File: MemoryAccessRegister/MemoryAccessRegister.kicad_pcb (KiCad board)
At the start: 2 copper layers, 75.8 x 38.8 mm, 20 parts, among them J1 Conn_01x04_Pin, J2 Conn_01x04_Pin, J3 Conn_01x06_Pin, SW1 SW_SPDT, U1 CD74HCT258E, U3 74LS173

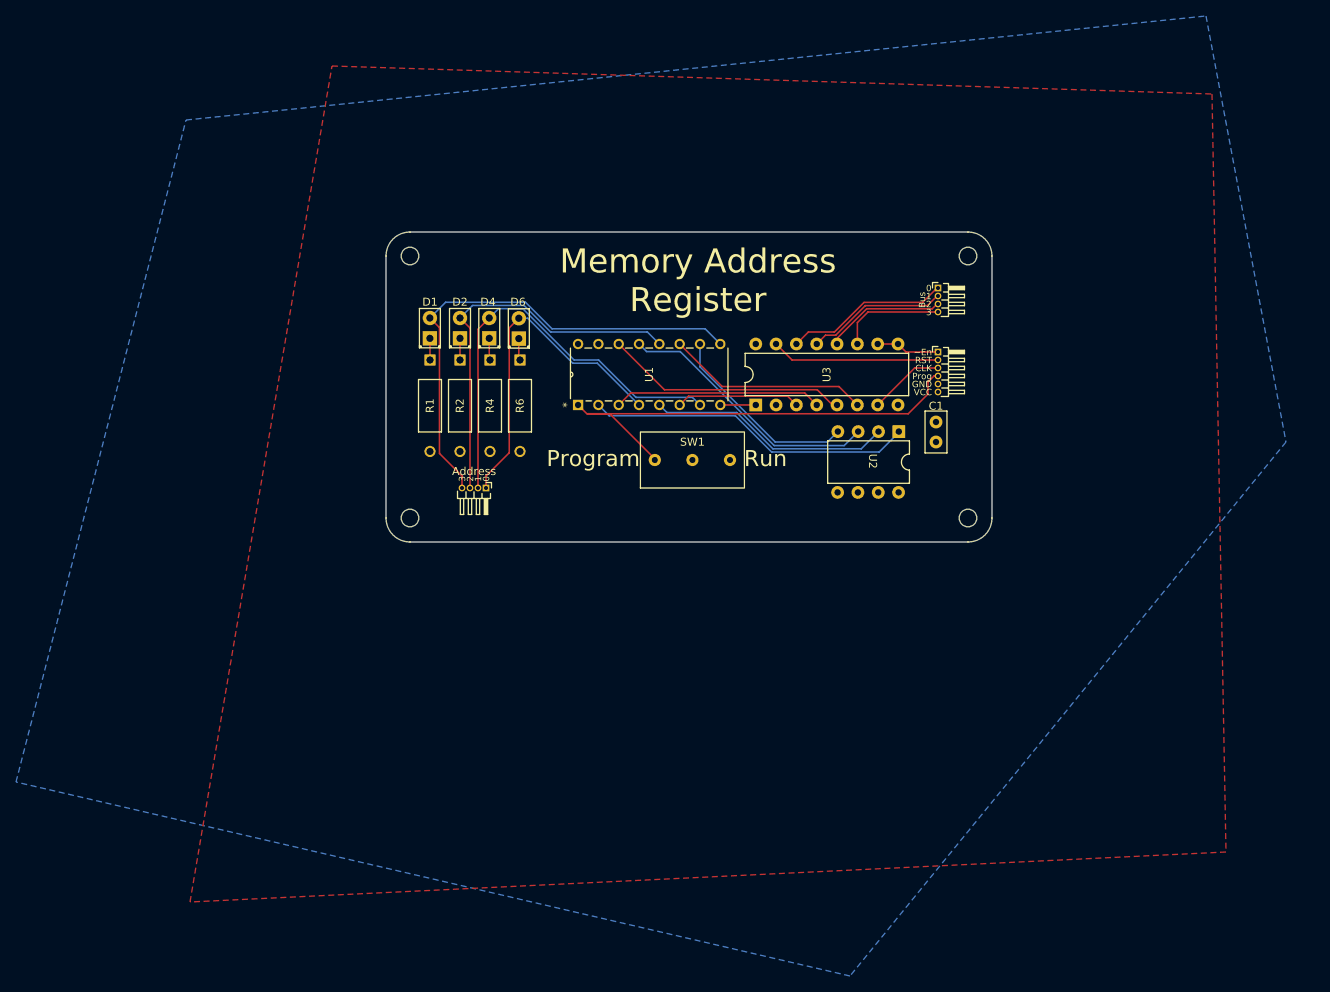
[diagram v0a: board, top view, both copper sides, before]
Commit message: Fixed LED and pin footprints for MAR and cleaned up the layout
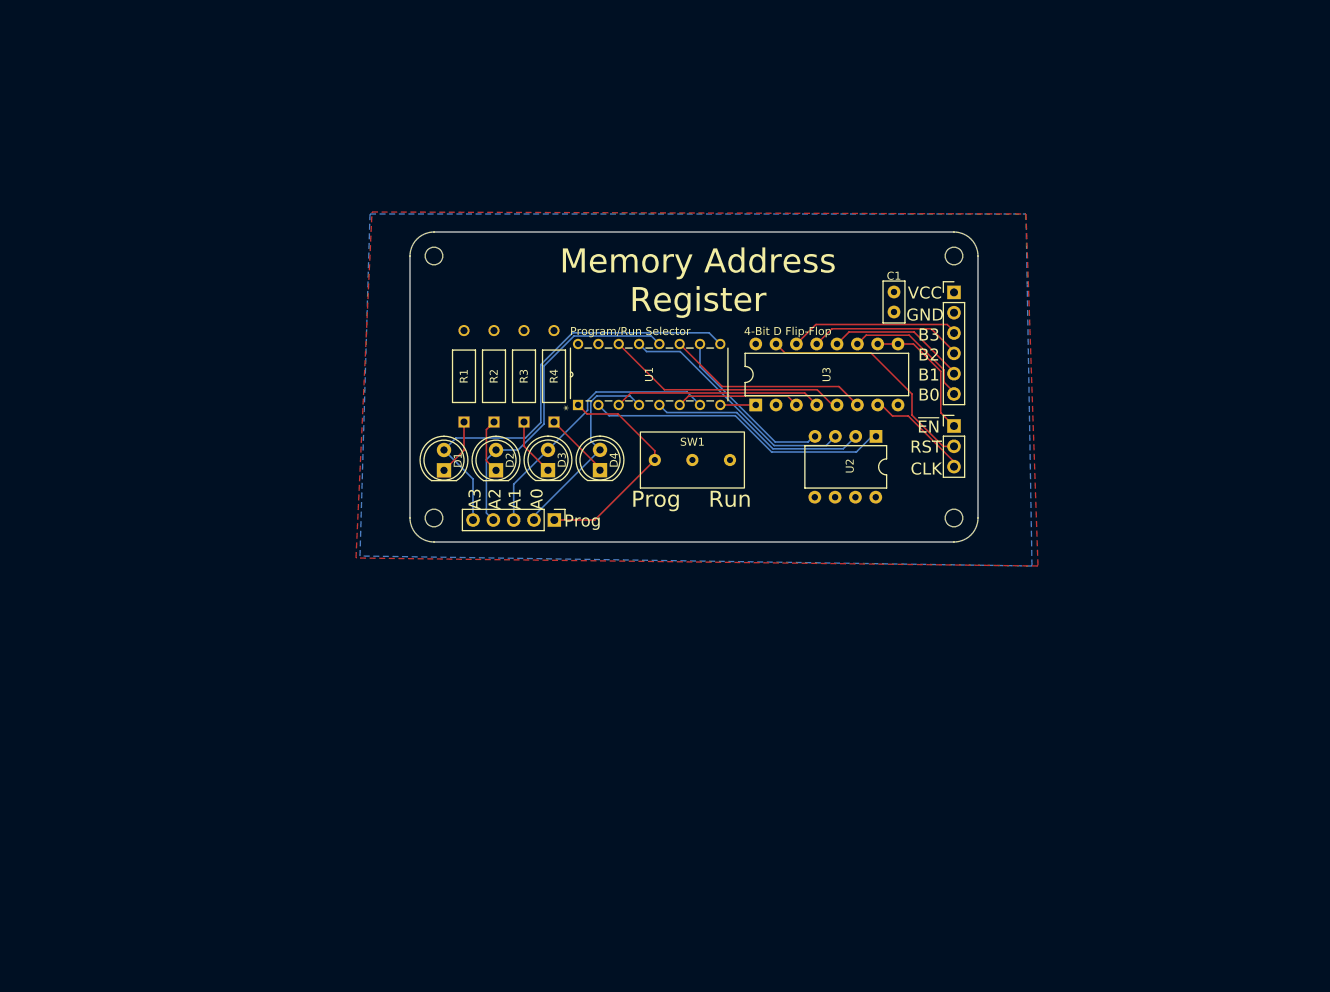
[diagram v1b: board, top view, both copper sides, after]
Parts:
- removed J1: Conn_01x04_Pin, Connector_PinHeader_1.00mm:PinHeader_1x04_P1.00mm_Horizontal
- removed the J2 at (228.2, 70.2)
- added J4: Conn_01x05_Pin, Connector_PinHeader_2.54mm:PinHeader_1x05_P2.54mm_Vertical, F.Cu at (180.3, 99.2)
- added J5: Conn_01x03_Pin, Connector_PinHeader_2.54mm:PinHeader_1x03_P2.54mm_Vertical, F.Cu at (230.2, 87.5)
- D1, D2: footprint LED_THT:LED_D2.0mm_W4.8mm_H2.5mm_FlatTop -> LED_THT:LED_D5.0mm
- D3: renamed from D4; footprint LED_THT:LED_D2.0mm_W4.8mm_H2.5mm_FlatTop -> LED_THT:LED_D5.0mm
- D4: renamed from D6; footprint LED_THT:LED_D2.0mm_W4.8mm_H2.5mm_FlatTop -> LED_THT:LED_D5.0mm
- J2: renamed from J3; footprint Connector_PinHeader_1.00mm:PinHeader_1x06_P1.00mm_Horizontal -> Connector_PinHeader_2.54mm:PinHeader_1x06_P2.54mm_Vertical
- moved D4 19.3 mm to (186.0, 93.0)
- moved D3 18.0 mm to (179.5, 93.0)
- moved D2 17.1 mm to (173.0, 93.0)
- moved C1 17.1 mm to (222.8, 70.8)
- moved D1 16.6 mm to (166.5, 93.0)
- moved R1 8.84 mm to (169.0, 87.0), turned to 90 degrees
- moved R2 8.84 mm to (172.8, 87.0), turned to 90 degrees
- moved R3 8.84 mm to (176.5, 87.0), turned to 90 degrees
- moved R4 8.84 mm to (180.2, 87.0), turned to 90 degrees
- moved J2 7.71 mm to (230.2, 70.8)
- moved REF** 3.00 mm to (165.2, 66.2)
- moved REF** 3.00 mm to (165.3, 99.0)
- moved U2 2.91 mm to (217.2, 92.5)
- moved REF** 1.75 mm to (230.2, 99.0)
- moved REF** 1.75 mm to (230.2, 66.2)
- renumbered R4 to R3, R6 to R4
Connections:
- J2 pad 1: /~En -> +5V
- J2 pad 2: /RST -> GND
- J2 pad 3: /CLK -> /Bus 0
- J2 pad 4: /Program -> /Bus 1
- J2 pad 5: GND -> /Bus 2
- J2 pad 6: +5V -> /Bus 3
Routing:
- net /Program: track 59.1 -> 28.8 mm
- net /A1: track 53.6 -> 33.9 mm
- net /A0: track 42.4 -> 25.5 mm
- net /~En: track 7.95 -> 16.8 mm
- net /A2: track 49.3 -> 40.6 mm
- net /RST: track 21.1 -> 29.1 mm
- net /A3: track 62.2 -> 55.7 mm
- net Net-(D4-K): track 2.74 -> 8.41 mm
- net Net-(D3-K): track 2.75 -> 7.27 mm
- net Net-(D1-K): track 2.72 -> 7.08 mm
- net Net-(D2-K): track 2.71 -> 6.93 mm
- net /CLK: track 9.45 -> 13.1 mm
- net /Bus 3: track 13.2 -> 16.4 mm
- net /Prog 0: track 41.1 -> 37.9 mm
- net /Prog 2: track 33.4 -> 30.3 mm
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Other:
- board size 75.8 x 38.8 mm -> 71 x 38.8 mm
- board text added: "4-Bit D Flip-Flop"
- board text added: "A0"
- board text added: "A1"
- board text added: "A2"
- board text added: "A3"
- board text added: "B0"
- board text added: "B1"
- board text added: "B2"
- board text added: "B3"
- board text added: "Program/Run Selector"
- board text added: "~{EN}"
- board text removed: "0"
- board text removed: "1"
- board text removed: "2"
- board text removed: "3"
- board text removed: "Address"
- board text removed: "Bus"
- board text removed: "Program"
- board text removed: "~En"

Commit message: Fixed misrouted bus connections to MUX. MUX is inverting so adde inverterto invert back. Slide switch should be conencted to power and pulled to ground. Breadboard validated.
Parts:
- added R5: 1k, _DownloadFootprints:CF_series_Resistors_THT, F.Cu at (180.2, 75.6)
- added R6: 1k, _DownloadFootprints:CF_series_Resistors_THT, F.Cu at (263.1, 84.2)
- added R7: 1k, _DownloadFootprints:CF_series_Resistors_THT, F.Cu at (263.1, 88.4)
- added R8: 1k, _DownloadFootprints:CF_series_Resistors_THT, F.Cu at (263.1, 92.7)
- added R9: 1k, _DownloadFootprints:CF_series_Resistors_THT, F.Cu at (263.1, 97.0)
- added U1: SN74AC14N, _DownloadFootprints:6x_not, F.Cu at (258.2, 97.5)
- moved R1 4.00 mm to (165.0, 87.0)
- moved R2 4.00 mm to (168.8, 87.0)
- moved R3 4.00 mm to (172.5, 87.0)
- moved R4 4.00 mm to (176.2, 87.0)
- moved U3 1.17 mm to (216.1, 92.7), turned to 90 degrees
- renumbered J4 to J1, J5 to J3, U1 to U2, U2 to U3, U3 to U4
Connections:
- net Net-(U1-3B) renamed /B3
- net Net-(U1-4B) renamed /B2
- U2 pad 12: /A2 -> /~A2
- U2 pad 15: +5V -> GND
- U2 pad 3: Net-(U1-1B) -> /B0
- U2 pad 4: /A0 -> /~A0
- U2 pad 6: Net-(U1-2B) -> /B1
- U2 pad 7: /A1 -> /~A1
- U2 pad 9: /A3 -> /~A3
- U3 pad 1: /Prog 0 -> +5V
- U3 pad 2: /Prog 1 -> +5V
- U3 pad 3: /Prog 2 -> +5V
- U3 pad 4: /Prog 3 -> +5V
- U3 pad 5: GND -> /Prog 0
- U3 pad 6: GND -> /Prog 1
- U3 pad 7: GND -> /Prog 2
- U3 pad 8: GND -> /Prog 3
- U4 pad 3: Net-(U1-2B) -> /B0
- U4 pad 4: Net-(U1-1B) -> /B1
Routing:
- net Net-(U1-1B): track 26.0 -> 0.00 mm
- net /B0: track 0.00 -> 23.1 mm
- net /B1: track 0.00 -> 18.0 mm
- net Net-(U1-2B): track 15.5 -> 0.00 mm
- net Net-(D4-K): track 8.41 -> 12.2 mm
- net /Program: track 28.8 -> 32.2 mm
- net Net-(D3-K): track 7.27 -> 9.50 mm
- net Net-(D2-K): track 6.93 -> 7.80 mm

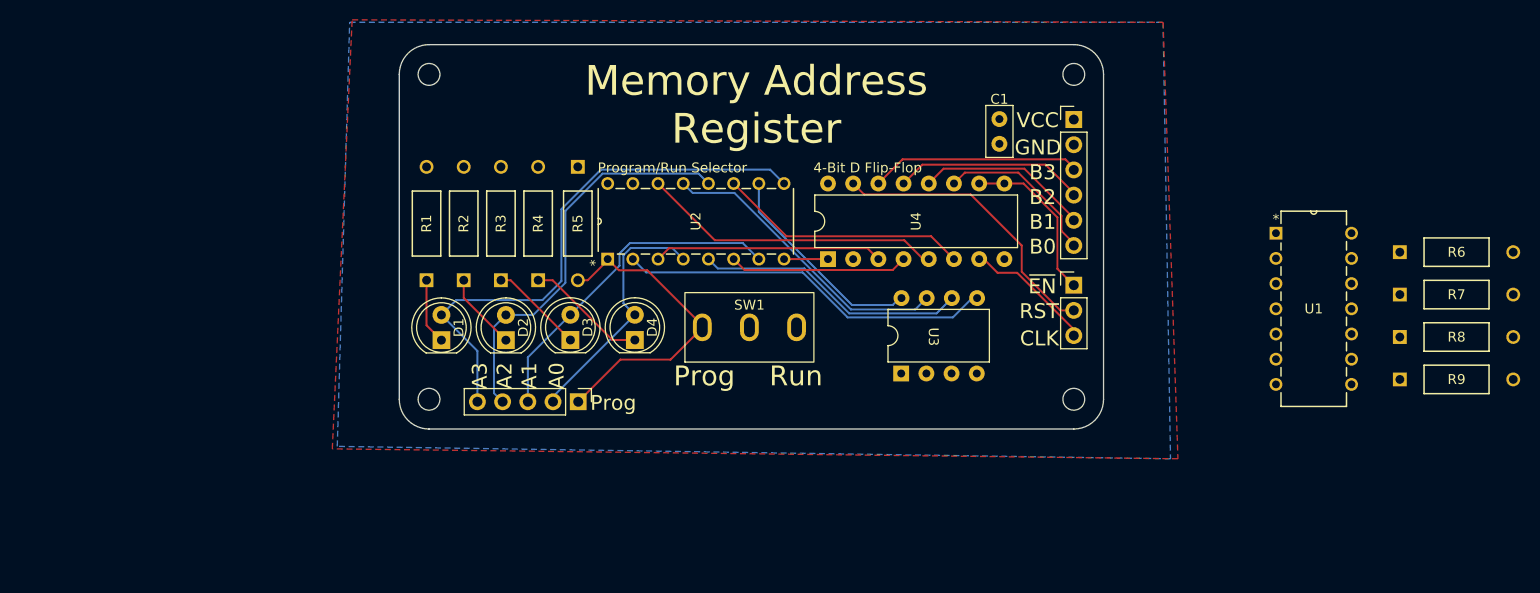
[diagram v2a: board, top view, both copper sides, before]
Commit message: MAR layout complete
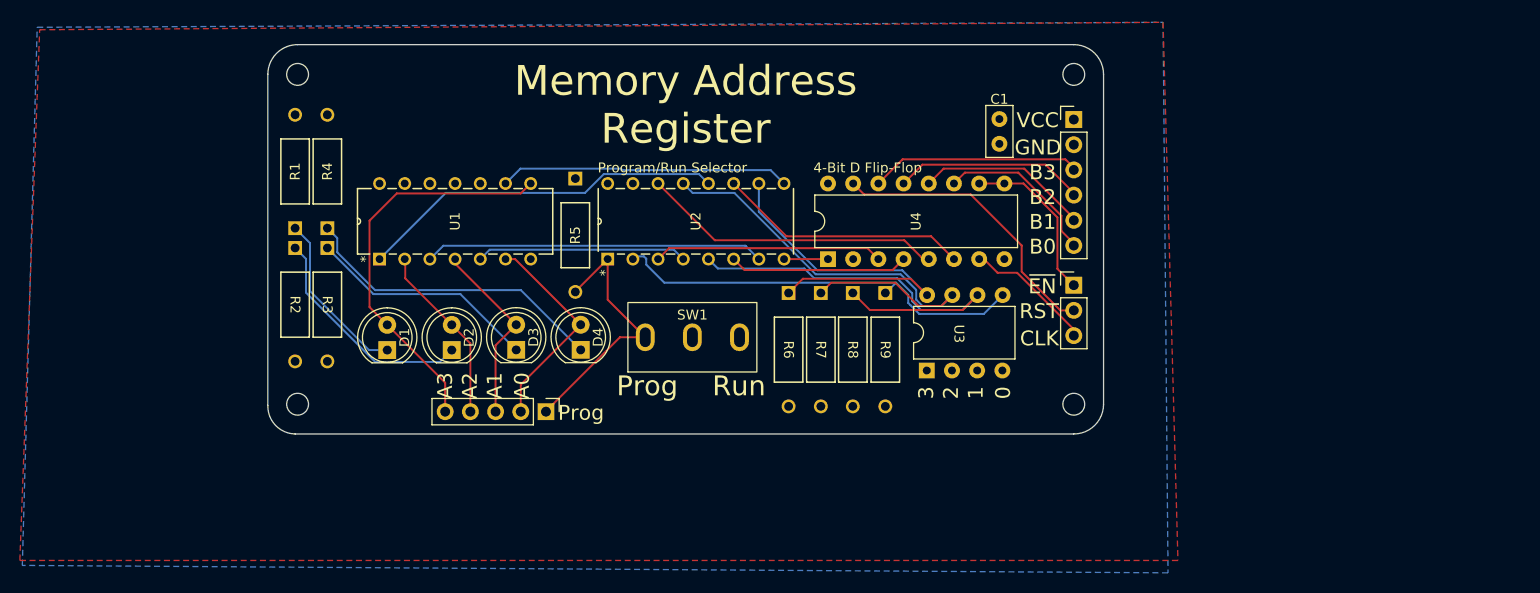
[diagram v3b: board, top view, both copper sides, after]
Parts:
- moved U1 85.2 mm to (175.5, 77.2), turned to 90 degrees
- moved R6 61.8 mm to (201.5, 88.3), turned to -90 degrees
- moved R7 58.4 mm to (204.8, 88.3), turned to -90 degrees
- moved R8 55.3 mm to (208.0, 88.3), turned to -90 degrees
- moved R9 52.6 mm to (211.2, 88.3), turned to -90 degrees
- moved R4 21.9 mm to (155.0, 81.8)
- moved R3 17.8 mm to (155.0, 83.8), turned to -90 degrees
- moved R2 17.3 mm to (151.8, 83.8), turned to -90 degrees
- moved R1 14.3 mm to (151.8, 81.8)
- moved REF** 13.3 mm to (152.0, 99.5)
- moved REF** 13.3 mm to (152.0, 66.2)
- moved SW1 5.84 mm to (191.8, 92.8)
- moved D1 5.55 mm to (161.0, 94.0)
- moved D2 5.55 mm to (167.5, 94.0)
- moved D3 5.55 mm to (174.0, 94.0)
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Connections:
- U1 pad 1: /~A0 -> /~A2
- U1 pad 2: /A0 -> /A2
- U1 pad 5: /~A2 -> /~A0
- U1 pad 6: /A2 -> /A0
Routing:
- net /~A2: track 0.00 -> 37.1 mm
- net /~A1: track 0.00 -> 34.3 mm
- net /~A3: track 0.00 -> 29.4 mm
- net /A2: track 40.6 -> 18.1 mm
- net /~A0: track 0.00 -> 21.2 mm
- net Net-(D4-K): track 12.2 -> 31.5 mm
- net /Prog 2: track 30.3 -> 48.4 mm
- net /Prog 3: track 21.4 -> 38.5 mm
- net /Prog 1: track 27.5 -> 44.2 mm
- net /A3: track 55.7 -> 40.2 mm
- net Net-(D2-K): track 7.80 -> 23.0 mm
- net /A1: track 33.9 -> 18.8 mm
- net Net-(D3-K): track 9.50 -> 23.3 mm
- net Net-(D1-K): track 6.66 -> 17.2 mm
- net /Prog 0: track 37.9 -> 42.9 mm
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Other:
- board size 71 x 38.8 mm -> 84.3 x 39.2 mm
- board text added: "0"
- board text added: "1"
- board text added: "2"
- board text added: "3"
